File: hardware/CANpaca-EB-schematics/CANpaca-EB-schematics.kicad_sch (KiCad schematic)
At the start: 85 parts

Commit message: more stuff + todo added
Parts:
- added C? (x6): 0.1uF, Capacitor_SMD:C_0603_1608Metric, symbol Device:C
- added C?: 2.2uF, Capacitor_SMD:C_0603_1608Metric, symbol Device:C
- added J?: Conn_01x02_Male, symbol Connector:Conn_01x02_Male
- added J?: A2501WV-4P, kicad-parts:A2501WV-4P, symbol keyboard_parts:A2501WV-4P
- added L?: 120R, symbol Device:L
- added R? (x3): 4.7K, Resistor_SMD:R_0603_1608Metric, symbol Device:R
- added R?: NC, Resistor_SMD:R_0603_1608Metric, symbol Device:R
- added R?: 430R, Resistor_SMD:R_0603_1608Metric, symbol Device:R
- added R? (x4): 10K, Resistor_SMD:R_0603_1608Metric, symbol Device:R
- added R?: 4.3K, Resistor_SMD:R_0603_1608Metric, symbol Device:R
- added R?: 1K, Resistor_SMD:R_0603_1608Metric, symbol Device:R
- added SW?: SW_DIP_x04, symbol Switch:SW_DIP_x04
- added U?: ADXL343, Package_LGA:LGA-14_3x5mm_P0.8mm_LayoutBorder1x6y, symbol Sensor_Motion:ADXL343
- added U?: MAX31865xTP, Package_DFN_QFN:TQFN-20-1EP_5x5mm_P0.65mm_EP3.25x3.25mm, symbol Sensor_Temperature:MAX31865xTP
- added U?: W25Q16, Package_SON:WSON-8-1EP_6x5mm_P1.27mm_EP3.4x4.3mm, symbol keyboard_parts:W25Q16
- added U?: SN74LVC1G32DVBR, Package_TO_SOT_SMD:SOT-23-5, symbol keyboard_parts:SN74LVC1G32DVBR
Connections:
- net 3V3: now also C?.1, C?.1, C?.1, C?.2, C?.2, L?.1, R?.1, R?.2, R?.2, R?.2, R?.2, R?.2, R?.2, R?.2, U?.1 (Vdd_I/O), U?.19 (DVDD), U?.5 (VCC), U?.6 (Vs), U?.8 (VCC)
- net CS_ADXL: now also R?.1, U?.1 (Y), U?.7 (~{CS})
- net CS_MAX: now also R?.1, U?.13 (~{CS})
- net GND: now also C?.1, C?.1, C?.2, C?.2, C?.2, J?.2 (Pin_2), U?.10 (GND), U?.11 (RES), U?.15 (DGND), U?.16 (GND), U?.2 (GND), U?.21 (GND), U?.3 (GND), U?.4 (GND), U?.4 (GND), U?.5 (GND), U?.6 (FORCE2)
- net MISO: now also R?.1, U?.12 (SDO/ADDR), U?.14 (SDO)
- net MOSI: now also R?.1, U?.11 (SDI), U?.2 (B)
- net QSPI_SCLK: now also U?.6 (CLK)
- net QSPI_SD0: now also U?.5 (DI(IO0))
- net QSPI_SD1: now also U?.2 (DO(IO1))
- net QSPI_SD2: now also U?.3 (IO2)
- net QSPI_SD3: now also U?.7 (IO3)
- net QSPI_SS: now also R?.2, R?.2, U?.1 (~{CS})
- net SCK: now also R?.1, R?.1, U?.12 (SCLK), U?.14 (SCL/SCLK)
- new net: R?.2, R?.2, U?.1 (BIAS), U?.2 (REFIN+)
- new net: C?.2, L?.2, U?.20 (VDD)
- new net: J?.1 (Pin_1), R?.1
- new net 4300R: R?.1, SW?.1
- new net 430R: R?.1, SW?.2
- new net FORCE_N: J?.4, SW?.3, U?.9 (FORCE-)
- new net FORCE_P: J?.1, SW?.4, U?.5 (FORCE+)
- new net ISENSOR: SW?.7, SW?.8, U?.3 (REFIN-), U?.4 (ISENSOR)
- new net MOSI_2: R?.1, U?.1 (Y), U?.13 (SDA/SDI/SDIO)
- new net RTDIN_N: C?.2, J?.3, SW?.6, U?.8 (RTDIN-)
- new net RTDIN_P: C?.1, J?.2, SW?.5, U?.7 (RTDIN+)
- no-connect marks 13 -> 18
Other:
- note added: "Todo: driver bltouch runout rgb th0"
- moved on the sheet: C?, D?, J?, Q?, R?, U?

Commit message: finished schematics
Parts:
- added C10: 470nF, Capacitor_SMD:C_0603_1608Metric, symbol Device:C
- added C11: 4.7uF, Capacitor_SMD:C_0603_1608Metric, symbol Device:C
- added C12: 100uF, symbol Device:C_Polarized_US
- added C13, C14, C16, C17, C52, C55, C6, C8: 0.1uF, Capacitor_SMD:C_0603_1608Metric, symbol Device:C
- added C50: 1uF, Capacitor_SMD:C_0603_1608Metric, symbol Device:C
- added C7: 22nF, Capacitor_SMD:C_0603_1608Metric, symbol Device:C
- added D7: BAT54S, Package_TO_SOT_SMD:SOT-23, symbol Diode:BAT54S
- added J13, J16: A2501WV-3P, kicad-parts:A2501WV-3P, symbol keyboard_parts:A2501WV-3P
- added J14, J18: A2501WV-5P, kicad-parts:A2501WV-5P, symbol keyboard_parts:A2501WV-5P
- added J15: Conn_01x02_Male, symbol Connector:Conn_01x02_Male
- added J17: A2501WV-2P, kicad-parts:A2501WV-2P, symbol keyboard_parts:A2501WV-2P
- added J8: A2501WV-4P, kicad-parts:A2501WV-4P, symbol keyboard_parts:A2501WV-4P
- added R11, R12: 0R, Resistor_SMD:R_0603_1608Metric, symbol Device:R
- added R30, R37: 4.7K, Resistor_SMD:R_0603_1608Metric, symbol Device:R
- added R33, R36: 2.37K, Resistor_SMD:R_0603_1608Metric, symbol Device:R
- added R38: 4.12K, Resistor_SMD:R_0603_1608Metric, symbol Device:R
- added R39: 10K, Resistor_SMD:R_0603_1608Metric, symbol Device:R
- added R8: 2R2, Resistor_SMD:R_0603_1608Metric, symbol Device:R
- added U3: TMC2130-LA, Package_DFN_QFN:QFN-36-1EP_5x6mm_P0.5mm_EP3.6x4.1mm, symbol Driver_Motor:TMC2130-LA
- gave numbers to parts that had none: 111
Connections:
- net 3V3: now also C55.2, C8.2, D7.2, J15.1 (Pin_1), J15.2 (Pin_2), J16.1, J18.5, R30.2, R37.2, R38.2, R39.1, U3.8 (VCC_IO)
- net 5V: now also C50.1, J13.1, J14.2
- net CS_E: now also U3.2 (~{CS}_CFG3)
- net DC_IN: now also C12.1, C13.2, C14.2, C6.1, U3.16 (VS), U3.30 (VSA), U3.31 (VS)
- net DIAG1_E: now also U3.21 (DIAG1)
- net DIR_E: now also U3.7 (DIR)
- net EN_E: now also U3.22 (~{DRV_EN}_CFG6)
- net GND: now also C54.1, C10.1, C11.1, C12.2, C13.1, C14.1, C16.2, C17.2, C50.2, C52.2, C55.1, C8.1, D7.1, J13.2, J14.1, J14.4, J16.2, J17.1, J18.3, R11.1, R12.1, U3.1 (CLK), U3.11 (NC), U3.12 (GNDP), U3.24 (GNDA), U3.35 (GNDP), U3.36 (TST_MODE), U3.37 (EP)
- net MISO: now also U3.5 (SDO_CFG0)
- net MOSI: now also U3.4 (SDI_CFG1)
- net PROBE: now also J14.5, R30.1
- net RGB: now also J13.3
- net RUNOUT: now also J16.3
- net SCK: now also U3.3 (SCK_CFG2)
- net SERVO: now also J14.3
- net STEP_E: now also U3.6 (STEP)
- net SWCLK: now also J18.2
- net SWDIO: now also J18.4, R39.2
- net TH_0: now also C52.1, R33.1
- net RUN: now reaches C51.2, R29.1, SW2.2, U10.26 (RUN)
- net RUN: now also J18.1
- new net: C16.1, R11.2, U3.33 (BRA)
- new net: C10.2, R8.1, U3.26 (VCC)
- new net: C11.2, R8.2, U3.25 (5VOUT)
- new net: D7.3, R33.2, R36.1
- new net: J17.2, R36.2, R37.1, R38.1
- new net: C17.1, R12.2, U3.14 (BRB)
- new net: J8.3, U3.13 (OB1)
- new net: J8.4, U3.15 (OB2)
- new net: C7.1, U3.27 (CPO)
- new net: C7.2, U3.28 (CPI)
- new net: C6.2, U3.29 (VCP)
- new net MOTOR_A1: J8.2, U3.34 (OA1)
- new net MOTOR_A2: J8.1, U3.32 (OA2)
- no-connect marks 18 -> 24
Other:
- note added: "5V to 3.3V"
- note added: "Accelerometer"
- note added: "BLTouch"
- note added: "CAN"
- note added: "DC to 5V"
- note added: "Debug"
- note added: "Fans"
- note added: "Flash"
- note added: "Hotend"
- note added: "RGB"
- note added: "RP2040"
- note added: "RTD-to-Digital"
- note added: "Runout"
- note added: "TMC2130 driver"
- note added: "Thermistor"
- note added: "USB"
- note removed: "Todo: driver bltouch runout rgb th0"
- moved on the sheet: C1, C15, C18, C19, C2, C20, C21, C22, C23, C24, C25, C26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

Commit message: finished pcb
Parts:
- removed C24: 4.7uF, Capacitor_SMD:C_0603_1608Metric, symbol Device:C
- removed C55: 0.1uF, Capacitor_SMD:C_0603_1608Metric, symbol Device:C
- removed F2: 1.5A, symbol Device:Fuse
- removed J1: Conn_01x03_Male, Connector_PinHeader_2.54mm:PinHeader_1x03_P2.54mm_Vertical, symbol Connector:Conn_01x03_Male
- removed J10, J15, J3: Conn_01x02_Male, symbol Connector:Conn_01x02_Male
- removed J18: A2501WV-5P, kicad-parts:A2501WV-5P, symbol keyboard_parts:A2501WV-5P
- removed R39: 10K, Resistor_SMD:R_0603_1608Metric, symbol Device:R
- removed SW1: SW_DIP_x04, symbol Switch:SW_DIP_x04
- removed SW2: SW_PUSH, symbol keyboard_parts:SW_PUSH
- removed U5: AMS1117, Package_TO_SOT_SMD:SOT-223, symbol keyboard_parts:LDO_REGULATOR
- added SW1: SW_DIP_x08, Button_Switch_SMD:SW_DIP_SPSTx08_Slide_Copal_CHS-08B_W7.62mm_P1.27mm, symbol Switch:SW_DIP_x08
- added U5: AMS1117-3.3, Package_TO_SOT_SMD:SOT-223-3_TabPin2, symbol Regulator_Linear:AMS1117
- C12: footprint (none) -> Capacitor_SMD:CP_Elec_10x14.3
- C31: value 4.7uF -> 22uF
- D1, D3: footprint (none) -> Diode_SMD:D_SOD-323
- D4: footprint (none) -> Diode_SMD:D_SOD-123
- D5: footprint (none) -> Diode_SMD:D_SOD-123F
- F1: footprint (none) -> Fuse:Fuse_BelFuse_0ZRE0005FF_L8.3mm_W3.8mm
- J12: footprint kicad-parts:A2501WV-4P -> kicad-parts:A1250WV-4P
- J13, J16: footprint kicad-parts:A2501WV-3P -> kicad-parts:A1250WV-3P
- J14: footprint kicad-parts:A2501WV-5P -> kicad-parts:A1250WV-5P
- J6: footprint (none) -> kicad-parts:KF350-2P
- J9: footprint GCT_USB4110-GF-A_REVB -> kicad-parts:GCT_USB4110-GF-A_REVB
- L2, L3: footprint (none) -> Inductor_SMD:L_0805_2012Metric
- R22: value 1.5K -> 1K
- U6: footprint Package_SON:WSON-8-1EP_6x5mm_P1.27mm_EP3.4x4.3mm -> Package_SO:SOIC-8_3.9x4.9mm_P1.27mm
- Y1: footprint (none) -> Crystal:Crystal_SMD_3225-4Pin_3.2x2.5mm
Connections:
- net 3V3: now also SW1.4, U5.2 (VO); no longer R38.2
- net 4300R: now also SW1.5
- net 430R: now also SW1.6
- net 5V: now also U5.3 (VI)
- net CAN_P: now also SW1.15
- net CS_E: now also U10.12 (GPIO9); no longer U10.11 (GPIO8)
- net DC_5V: now also C32.2, L2.2, R19.2
- net DIAG1_E: now also U10.8 (GPIO6); no longer U10.12 (GPIO9)
- net DIR_E: now also U10.5 (GPIO3); no longer U10.8 (GPIO6)
- net EN_E: now also U10.4 (GPIO2); no longer U10.9 (GPIO7)
- net FORCE_N: now also SW1.7
- net FORCE_P: now also SW1.8
- net GND: now also SW1.1, SW1.3, U5.1 (ADJ)
- net ISENSOR: now also SW1.11, SW1.12
- net MISO: now also U10.7 (GPIO5); no longer U10.6 (GPIO4)
- net MOSI: now also U10.9 (GPIO7); no longer U10.5 (GPIO3)
- net MOSI_2: now also U9.4 (Y); no longer U9.1 (Y)
- net RGB: now also U10.28 (GPIO17); no longer U10.29 (GPIO18)
- net RTDIN_N: now also SW1.10
- net RTDIN_P: now also SW1.9
- net RUN: now also SW1.16
- net RUNOUT: now also U10.29 (GPIO18); no longer U10.28 (GPIO17)
- net SCK: now also U10.11 (GPIO8); no longer U10.4 (GPIO2)
- net STEP_E: now also U10.6 (GPIO4); no longer U10.7 (GPIO5)
- net at C15.2, D3.1 (K), J4.2 (Pin_2)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: now also C5.2, D1.1 (K), J2.1
- net CAN_OUT: now reaches R4.1
- net CAN_OUT: now also SW1.2
- net BOOT_IN: now reaches R15.1
- net BOOT_IN: now also SW1.14
- new net THO_IN: R38.2, SW1.13
- no-connect marks 24 -> 22
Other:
- note removed: "Debug"
- moved on the sheet: C1, C2, C3, C31, C33, C4, D2, D6, J4, R22, R3, R4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

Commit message: added schematic pdf
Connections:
- net DIAG1_E: now also U10.7 (GPIO5); no longer U10.8 (GPIO6)
- net MISO: now also U10.8 (GPIO6); no longer U10.7 (GPIO5)
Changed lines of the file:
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@@
+    (stroke (width 0) (type default) (color 0 0 0 0))
+  )
+  (wire (pts (xy 267.97 33.02) (xy 269.24 33.02))
+    (stroke (width 0) (type default) (color 0 0 0 0))
+  )
+  (wire (pts (xy 342.9 54.61) (xy 344.17 54.61))
+    (stroke (width 0) (type default) (color 0 0 0 0))
+  )
+  (wire (pts (xy 43.18 34.29) (xy 43.18 36.83))
+    (stroke (width 0) (type default) (color 0 0 0 0))
+  )
+  (wire (pts (xy 200.66 204.47) (xy 201.93 204.47))
+    (stroke (width 0) (type default) (color 0 0 0 0))
+  )
+  (wire (pts (xy 298.45 93.98) (xy 298.45 96.52))
+    (stroke (width 0) (type default) (color 0 0 0 0))
+  )
+  (wire (pts (xy 179.07 209.55) (xy 180.34 209.55))
+    (stroke (width 0) (type default) (color 0 0 0 0))
+  )
+  (wire (pts (xy 81.28 100.33) (xy 83.82 100.33))
+    (stroke (width 0) (type default) (color 0 0 0 0))
+  )
+  (wire (pts (xy 172.72 68.58) (xy 172.72 71.12))
+    (stroke (width 0) (type default) (color 0 0 0 0))
+  )
+  (wire (pts (xy 266.7 191.77) (xy 266.7 199.39))
+    (stroke (width 0) (type default) (color 0 0 0 0))
+  )
+  (wire (pts (xy 190.5 101.6) (xy 191.77 101.6))
+    (stroke (width 0) (type default) (color 0 0 0 0))
+  )
+  (wire (pts (xy 45.72 154.94) (xy 44.45 154.94))
+    (stroke (width 0) (type default) (color 0 0 0 0))
+  )
+  (wire (pts (xy 313.69 158.75) (xy 314.96 158.75))
+    (stroke (width 0) (type default) (color 0 0 0 0))
+  )
+  (wire (pts (xy 340.36 234.95) (xy 340.36 236.22))
+    (stroke (width 0) (type default) (color 0 0 0 0))
+  )
+  (wire (pts (xy 69.85 223.52) (xy 69.85 224.79))
+    (stroke (width 0) (type default) (color 0 0 0 0))
+  )
+  (polyline (pts (xy 114.3 132.08) (xy 15.24 132.08))
+    (stroke (width 0) (type default) (color 0 0 0 0))
+  )
+  (wire (pts (xy 279.4 93.98) (xy 278.13 93.98))
+    (stroke (width 0) (type default) (color 0 0 0 0))
+  )
+  (wire (pts (xy 83.82 97.79) (xy 83.82 93.98))
+    (stroke (width 0) (type default) (color 0 0 0 0))
+  )
+  (wire (pts (xy 186.69 167.64) (xy 186.69 172.72))
+    (stroke (width 0) (type default) (color 0 0 0 0))
+  )
+  (wire (pts (xy 162.56 71.12) (xy 163.83 71.12))
+    (stroke (width 0) (type default) (color 0 0 0 0))
+  )
+  (polyline (pts (xy 304.8 46.99) (xy 368.3 46.99))
+    (stroke (width 0) (type default) (color 0 0 0 0))
+  )
+  (wire (pts (xy 191.77 95.25) (xy 193.04 95.25))
+    (stroke (width 0) (type default) (color 0 0 0 0))
+  )
+  (wire (pts (xy 73.66 33.02) (xy 73.66 38.1))
+    (stroke (width 0) (type default) (color 0 0 0 0))
+  )
+  (wire (pts (xy 347.98 140.97) (xy 350.52 140.97))
+    (stroke (width 0) (type default) (color 0 0 0 0))
+  )
+  (wire (pts (xy 41.91 161.29) (xy 44.45 161.29))
+    (stroke (width 0) (type default) (color 0 0 0 0))
+  )
+  (wire (pts (xy 63.5 170.18) (xy 63.5 176.53))
+    (stroke (width 0) (type default) (color 0 0 0 0))
+  )
+  (wire (pts (xy 336.55 86.36) (xy 337.82 86.36))
+    (stroke (width 0) (type default) (color 0 0 0 0))
+  )
+  (wire (pts (xy 266.7 207.01) (xy 266.7 203.2))
+    (stroke (width 0) (type default) (color 0 0 0 0))
+  )
+  (wire (pts (xy 297.18 93.98) (xy 298.45 93.98))
+    (stroke (width 0) (type default) (color 0 0 0 0))
+  )
+  (wire (pts (xy 314.96 196.85) (xy 295.91 196.85))
+    (stroke (width 0) (type default) (color 0 0 0 0))
+  )
+  (wire (pts (xy 152.4 205.74) (xy 153.67 205.74))
+    (stroke (width 0) (type default) (color 0 0 0 0))
+  )
+  (wire (pts (xy 285.75 208.28) (xy 285.75 203.2))
     (stroke (width 0) (type default) (color 0 0 0 0))
   )
@@
     (stroke (width 0) (type default) (color 0 0 0 0))
   )
-  (wire (pts (xy 267.97 33.02) (xy 269.24 33.02))
-    (stroke (width 0) (type default) (color 0 0 0 0))
-  )
-  (wire (pts (xy 342.9 54.61) (xy 344.17 54.61))
-    (stroke (width 0) (type default) (color 0 0 0 0))
-  )
-  (wire (pts (xy 43.18 34.29) (xy 43.18 36.83))
-    (stroke (width 0) (type default) (color 0 0 0 0))
-  )
-  (wire (pts (xy 200.66 204.47) (xy 201.93 204.47))
-    (stroke (width 0) (type default) (color 0 0 0 0))
-  )
-  (wire (pts (xy 298.45 93.98) (xy 298.45 96.52))
-    (stroke (width 0) (type default) (color 0 0 0 0))
-  )
-  (wire (pts (xy 179.07 209.55) (xy 180.34 209.55))
-    (stroke (width 0) (type default) (color 0 0 0 0))
-  )
-  (wire (pts (xy 81.28 100.33) (xy 83.82 100.33))
-    (stroke (width 0) (type default) (color 0 0 0 0))
-  )
-  (wire (pts (xy 172.72 68.58) (xy 172.72 71.12))
-    (stroke (width 0) (type default) (color 0 0 0 0))
-  )
-  (wire (pts (xy 266.7 191.77) (xy 266.7 199.39))
-    (stroke (width 0) (type default) (color 0 0 0 0))
-  )
-  (wire (pts (xy 190.5 101.6) (xy 191.77 101.6))
-    (stroke (width 0) (type default) (color 0 0 0 0))
-  )
-  (wire (pts (xy 45.72 154.94) (xy 44.45 154.94))
-    (stroke (width 0) (type default) (color 0 0 0 0))
-  )
-  (wire (pts (xy 313.69 158.75) (xy 314.96 158.75))
-    (stroke (width 0) (type default) (color 0 0 0 0))
-  )
-  (wire (pts (xy 340.36 234.95) (xy 340.36 236.22))
-    (stroke (width 0) (type default) (color 0 0 0 0))
-  )
-  (wire (pts (xy 69.85 223.52) (xy 69.85 224.79))
-    (stroke (width 0) (type default) (color 0 0 0 0))
-  )
-  (polyline (pts (xy 114.3 132.08) (xy 15.24 132.08))
-    (stroke (width 0) (type default) (color 0 0 0 0))
-  )
-  (wire (pts (xy 279.4 93.98) (xy 278.13 93.98))
-    (stroke (width 0) (type default) (color 0 0 0 0))
-  )
-  (wire (pts (xy 83.82 97.79) (xy 83.82 93.98))
-    (stroke (width 0) (type default) (color 0 0 0 0))
-  )
-  (wire (pts (xy 186.69 167.64) (xy 186.69 172.72))
-    (stroke (width 0) (type default) (color 0 0 0 0))
-  )
-  (wire (pts (xy 162.56 71.12) (xy 163.83 71.12))
-    (stroke (width 0) (type default) (color 0 0 0 0))
-  )
-  (polyline (pts (xy 304.8 46.99) (xy 368.3 46.99))
-    (stroke (width 0) (type default) (color 0 0 0 0))
-  )
-  (wire (pts (xy 191.77 95.25) (xy 193.04 95.25))
-    (stroke (width 0) (type default) (color 0 0 0 0))
-  )
-  (wire (pts (xy 73.66 33.02) (xy 73.66 38.1))
-    (stroke (width 0) (type default) (color 0 0 0 0))
-  )
-  (wire (pts (xy 347.98 140.97) (xy 350.52 140.97))
-    (stroke (width 0) (type default) (color 0 0 0 0))
-  )
-  (wire (pts (xy 41.91 161.29) (xy 44.45 161.29))
-    (stroke (width 0) (type default) (color 0 0 0 0))
-  )
-  (wire (pts (xy 63.5 170.18) (xy 63.5 176.53))
-    (stroke (width 0) (type default) (color 0 0 0 0))
-  )
-  (wire (pts (xy 336.55 86.36) (xy 337.82 86.36))
-    (stroke (width 0) (type default) (color 0 0 0 0))
-  )
-  (wire (pts (xy 266.7 207.01) (xy 266.7 203.2))
-    (stroke (width 0) (type default) (color 0 0 0 0))
-  )
-  (wire (pts (xy 297.18 93.98) (xy 298.45 93.98))
-    (stroke (width 0) (type default) (color 0 0 0 0))
-  )
-  (wire (pts (xy 314.96 196.85) (xy 295.91 196.85))
-    (stroke (width 0) (type default) (color 0 0 0 0))
-  )
-  (wire (pts (xy 152.4 205.74) (xy 153.67 205.74))
-    (stroke (width 0) (type default) (color 0 0 0 0))
-  )
-  (wire (pts (xy 285.75 208.28) (xy 285.75 203.2))
-    (stroke (width 0) (type default) (color 0 0 0 0))
-  )
   (wire (pts (xy 314.96 86.36) (xy 314.96 92.71))
     (stroke (width 0) (type default) (color 0 0 0 0))
@@
     (stroke (width 0) (type default) (color 0 0 0 0))
   )
+  (wire (pts (xy 365.76 163.83) (xy 367.03 163.83))
+    (stroke (width 0) (type default) (color 0 0 0 0))
+  )
   (wire (pts (xy 190.5 156.21) (xy 190.5 172.72))
     (stroke (width 0) (type default) (color 0 0 0 0))
@@
   )
   (wire (pts (xy 80.01 147.32) (xy 81.28 147.32))
-    (stroke (width 0) (type default) (color 0 0 0 0))
-  )
-  (wire (pts (xy 365.76 163.83) (xy 367.03 163.83))
     (stroke (width 0) (type default) (color 0 0 0 0))
   )
@@
     )
   )
-  (global_label "MISO" (shape input) (at 367.03 163.83 0) (fields_autoplaced)
-    (effects (font (size 1.27 1.27)) (justify left))
-    (property "Intersheet References" "${INTERSHEET_REFS}" (id 0) (at 374.0393 163.7506 0)
+  (global_label "MISO" (shape input) (at 367.03 166.37 0) (fields_autoplaced)
+    (effects (font (size 1.27 1.27)) (justify left))
+    (property "Intersheet References" "${INTERSHEET_REFS}" (id 0) (at 374.0393 166.2906 0)
       (effects (font (size 1.27 1.27)) (justify left) hide)
     )
@@
     )
   )
-  (global_label "DIAG1_E" (shape input) (at 367.03 166.37 0) (fields_autoplaced)
-    (effects (font (size 1.27 1.27)) (justify left))
-    (property "Intersheet References" "${INTERSHEET_REFS}" (id 0) (at 377.0026 166.2906 0)
-      (effects (font (size 1.27 1.27)) (justify left) hide)
-    )
+  (global_label "DIAG1_E" (shape input) (at 367.03 163.83 0) (fields_autoplaced)
+    (effects (font (size 1.27 1.27)) (justify left))
+    (property "Intersheet References" "${INTERSHEET_REFS}" (id 0) (at 377.0026 163.7506 0)
+      (effects (font (size 1.27 1.27)) (justify left) hide)
+    )

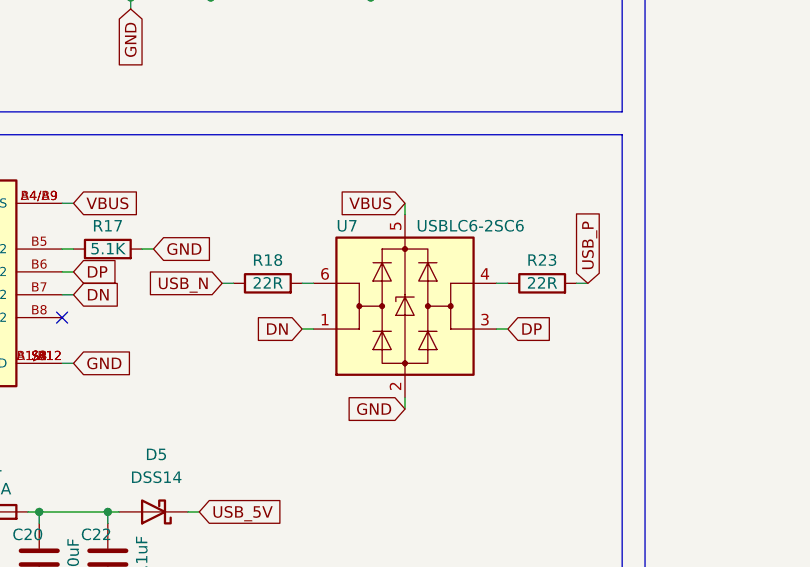
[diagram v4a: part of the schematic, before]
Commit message: fixed usb resistor
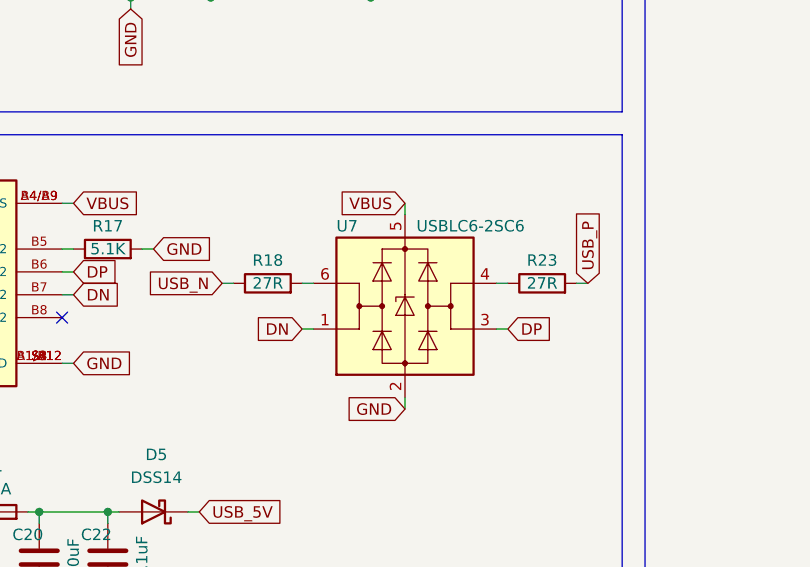
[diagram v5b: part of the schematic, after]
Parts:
- R18, R23: value 22R -> 27R
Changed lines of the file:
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@@
     (in_bom yes) (on_board yes)
     (property "Reference" "R23" (id 0) (at 205.74 201.93 90))
-    (property "Value" "22R" (id 1) (at 205.74 204.47 90))
+    (property "Value" "27R" (id 1) (at 205.74 204.47 90))
     (property "Footprint" "Resistor_SMD:R_0603_1608Metric" (id 2) (at 205.74 206.248 90)
       (effects (font (size 1.27 1.27)) hide)
@@
     (in_bom yes) (on_board yes)
     (property "Reference" "R18" (id 0) (at 175.26 201.93 90))
-    (property "Value" "22R" (id 1) (at 175.26 204.47 90))
+    (property "Value" "27R" (id 1) (at 175.26 204.47 90))
     (property "Footprint" "Resistor_SMD:R_0603_1608Metric" (id 2) (at 175.26 206.248 90)
       (effects (font (size 1.27 1.27)) hide)
@@
     )
     (path "/86c24caa-157e-47c9-a430-a6259a582c95"
-      (reference "R18") (unit 1) (value "22R") (footprint "Resistor_SMD:R_0603_1608Metric")
+      (reference "R18") (unit 1) (value "27R") (footprint "Resistor_SMD:R_0603_1608Metric")
     )
     (path "/4bbd0da2-bc15-48da-9b80-bfb2a6f587eb"
@@
     )
     (path "/2d53dc50-78ff-4921-94e4-a84c82efa0ea"
-      (reference "R23") (unit 1) (value "22R") (footprint "Resistor_SMD:R_0603_1608Metric")
+      (reference "R23") (unit 1) (value "27R") (footprint "Resistor_SMD:R_0603_1608Metric")
     )
     (path "/a2fbcfb7-591c-46db-b8bf-d37e22704016"
